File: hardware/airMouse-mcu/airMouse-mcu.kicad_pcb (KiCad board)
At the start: 2 copper layers, 126 parts, among them J1 DS1020-07-16VBT1A-R, J4 AT, J5 RADIO_PRG, J6 MCU_PRG, Q1 IRLML6346, SW50 KEY, SW51 KEY, SW52 KEY, SW53 KEY, SW54 KEY, SW55 KEY, SW56 KEY, SW57 KEY, SW58 KEY, SW59 KEY, SW60 KEY, U1 STM32G071RBTx, U2 AP1603, U3 ESP32-C3-WROOM-02U, U4 LSM6DS3

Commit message: add mouse pcb
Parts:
- removed D12: STBY, LED_SMD:LED_0603_1608Metric
- removed D13: BT, LED_SMD:LED_0603_1608Metric
- removed D43: LOW_BAT, LED_SMD:LED_0603_1608Metric
- removed R53, R54, R55, R56, R58, R59: 10k, Resistor_SMD:R_0603_1608Metric
- removed R57: 2k2, Resistor_SMD:R_0603_1608Metric
- removed R60, R61: 0R, Resistor_SMD:R_0603_1608Metric
- removed SW50, SW51, SW52, SW53, SW54, SW55, SW56, SW57, SW58, SW59, SW60: KEY, airMouseLib:TL3315NF100Q
- added D2: BT, LED_SMD:LED_0603_1608Metric, F.Cu at (123.4, 90.2)
- added D3: LOW_BAT, LED_SMD:LED_0603_1608Metric, F.Cu at (123.4, 92.8)
- added D4: STBY, LED_SMD:LED_0603_1608Metric, F.Cu at (123.4, 95.3)
- added J2: RADIO_PRG, Connector_JST:JST_ZH_S3B-ZR-SM4A-TF_1x03-1MP_P1.50mm_Horizontal, F.Cu at (131.1, 91.5)
- added J3: AT, Connector_JST:JST_ZH_S3B-ZR-SM4A-TF_1x03-1MP_P1.50mm_Horizontal, F.Cu at (131.1, 100.5)
- added SW1: KEY, airMouseLib:TL3315NF100Q, F.Cu at (149.8, 91.2)
- C11: value 100n -> 4u7; footprint Capacitor_SMD:C_0603_1608Metric -> Capacitor_SMD:C_0805_2012Metric
- C13, C9: value 100n -> 1u
- C15: value 100n -> 10u; footprint Capacitor_SMD:C_0603_1608Metric -> Capacitor_SMD:C_0805_2012Metric
- C2, C7: value 100n -> 47u; footprint Capacitor_SMD:C_0603_1608Metric -> Capacitor_SMD:CP_Elec_6.3x5.8
- C27: value 4u7 -> 100n; footprint Capacitor_SMD:C_0805_2012Metric -> Capacitor_SMD:C_0603_1608Metric
- C28, C30: value 1u -> 100n
- C3, C4: value 47u -> 100n; footprint Capacitor_SMD:CP_Elec_6.3x5.8 -> Capacitor_SMD:C_0603_1608Metric
- C32: value 10u -> 100n; footprint Capacitor_SMD:C_0805_2012Metric -> Capacitor_SMD:C_0603_1608Metric
- J1: value DS1020-07-16VBT1A-R -> MCU_PRG; footprint airMouseLib:DS1020-07-16VBT1A-R -> Connector_JST:JST_ZH_S5B-ZR-SM4A-TF_1x05-1MP_P1.50mm_Horizontal
- J4: value AT -> DS1020-07-16VBT1A-R; footprint Connector_JST:JST_ZH_S3B-ZR-SM4A-TF_1x03-1MP_P1.50mm_Horizontal -> airMouseLib:DS1020-07-16VBT1A-R
- J5: value RADIO_PRG -> DS1020-07-10VBT1A-R; footprint Connector_JST:JST_ZH_S3B-ZR-SM4A-TF_1x03-1MP_P1.50mm_Horizontal -> airMouseLib:DS1020-07-10VBT1A-R
- J6: value MCU_PRG -> Conn_01x04_MountingPin; footprint Connector_JST:JST_ZH_S5B-ZR-SM4A-TF_1x05-1MP_P1.50mm_Horizontal -> airMouseLib:DS1020-07-4VBT1A-R
- R1, R15, R2: value 100R -> 10k
- R10, R8: value 10k -> 4k7
- R12, R17: value 10k -> 2k2
- R13, R14: value 100R -> 2k2
- R18, R19, R20, R21, R22: value 10k -> 100R
- R3, R4: value 10k -> 0R
- R46, R47, R48: value 2k2 -> 10k
- R51, R52: value 4k7 -> 10k
- R6: value 10k -> 1k
- U1: value STM32G071RBTx -> LSM6DS3; footprint Package_QFP:LQFP-64_10x10mm_P0.5mm -> Package_LGA:LGA-14_3x2.5mm_P0.5mm_LayoutBorder3x4y
- U3: value ESP32-C3-WROOM-02U -> STM32G071RBTx; footprint RF_Module:ESP32-C3-WROOM-02U -> Package_QFP:LQFP-64_10x10mm_P0.5mm
- U4: value LSM6DS3 -> ESP32-C3-WROOM-02U; footprint Package_LGA:LGA-14_3x2.5mm_P0.5mm_LayoutBorder3x4y -> RF_Module:ESP32-C3-WROOM-02U
- moved TP1 107.4 mm to (122.9, 104.2)
- moved TP2 107.4 mm to (122.9, 107.2)
- moved C3 104.8 mm to (107.3, 92.6)
- moved C1 104.3 mm to (107.3, 90.1)
- moved C5 104.3 mm to (107.3, 97.7)
- moved J4 89.9 mm to (133.5, 138.2)
- moved R43 89.1 mm to (115.4, 121.7)
- moved R44 89.1 mm to (115.4, 124.2)
- moved R45 89.1 mm to (115.4, 126.7)
- moved C33 77.7 mm to (111.3, 126.7)
- moved C34 77.7 mm to (111.3, 129.2)
- moved C30 75.2 mm to (107.3, 131.7)
- moved C28 75.2 mm to (107.3, 126.7)
- moved C29 75.2 mm to (107.3, 129.2)
- moved C35 74.7 mm to (111.3, 131.7)
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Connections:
- C10 pad 1: /COL7 -> +3V3
- C11 pad 1: /COL5 -> +3V3
- C12 pad 1: /COL4 -> /ADC
- C13 pad 1: /COL3 -> /ESP_RST
- C14 pad 1: /COL2 -> +3V3
- C15 pad 1: /COL1 -> +3V3
- C16 pad 1: /mouse/MOUSE_RB -> /COL10
- C17 pad 1: /mouse/MOUSE_MB -> /COL9
- C18 pad 1: /mouse/MOUSE_LB -> /COL8
- C19 pad 1: /mouse/MOUSE_UP -> /COL7
- C2 pad 1: Net-(U2-REF) -> /BAT+
- C20 pad 1: /mouse/MOUSE_DN -> /COL6
- C21 pad 1: /mouse/MOUSE_FWD -> /COL5
- C22 pad 1: /mouse/MOUSE_BACK -> /COL4
- C23 pad 1: /mouse/MOUSE_DPI -> /COL3
- C24 pad 1: /mouse/MOUSE_PRC -> /COL2
- C25 pad 1: /mouse/MOUSE_HOME -> /COL1
- C26 pad 1: +3V3 -> /mouse/MOUSE_HOME
- C27 pad 1: +3V3 -> /mouse/MOUSE_PRC
- C28 pad 1: +3V3 -> /mouse/MOUSE_DPI
- C29 pad 1: Net-(U1-VREF+) -> /mouse/MOUSE_BACK
- C3 pad 1: /BAT+ -> +3V3
- C30 pad 1: /ESP_RST -> /mouse/MOUSE_FWD
- C31 pad 1: +3V3 -> /mouse/MOUSE_DN
- C32 pad 1: +3V3 -> /mouse/MOUSE_UP
- C33 pad 1: +3V3 -> /mouse/MOUSE_RB
- C34 pad 1: +3V3 -> /mouse/MOUSE_MB
- C35 pad 1: /BAT+ -> /mouse/MOUSE_LB
- C4 pad 1: +3V3 -> Net-(U2-REF)
- C6 pad 1: /COL6 -> +3V3
- C7 pad 1: /COL10 -> +3V3
- C8 pad 1: /COL9 -> Net-(U3-VREF+)
- C9 pad 1: /COL8 -> +3V3
- FB1 pad 2: Net-(U1-VREF+) -> Net-(U3-VREF+)
- J1 pad 1: /Keyboard/ROW5 -> +3V3
- J1 pad 2: /Keyboard/ROW4 -> /SWDCLK
- J1 pad 3: /Keyboard/ROW3 -> GND
- J1 pad 4: /Keyboard/ROW2 -> /SWDIO
- J1 pad 5: /Keyboard/ROW1 -> /RST
- J4 pad 1: /AT_MCU_TX -> /Keyboard/ROW5
- J4 pad 2: /AT_MCU_RX -> /Keyboard/ROW4
- J4 pad 3: GND -> /Keyboard/ROW3
- J5 pad 1: /PRG_ESP_RX -> GND
- J5 pad 2: /PRG_ESP_TX -> /mouse/HOME
- J5 pad 3: GND -> /mouse/PRECISION
- J6 pad 1: +3V3 -> GND
- J6 pad 2: /SWDCLK -> /mouse/BACK
- J6 pad 3: GND -> /mouse/FWD
- J6 pad 4: /SWDIO -> +3V3
- R1 pad 1: /Keyboard/KEY_ROW1 -> +3V3
- R1 pad 2: /Keyboard/ROW1 -> Net-(U1-CS)
- R10 pad 2: /Keyboard/COL8 -> /SCL
- R11 pad 2: /Keyboard/COL9 -> Net-(U4-IO8)
- R12 pad 1: +3V3 -> Net-(D2-K)
- R12 pad 2: /Keyboard/COL10 -> GND
- R13 pad 1: /Keyboard/KEY_ROW3 -> Net-(D3-K)
- R13 pad 2: /Keyboard/ROW3 -> GND
- R14 pad 1: /Keyboard/KEY_ROW4 -> Net-(D4-K)
- R14 pad 2: /Keyboard/ROW4 -> GND
- R15 pad 1: /Keyboard/KEY_ROW5 -> +3V3
- R15 pad 2: /Keyboard/ROW5 -> Net-(U4-IO2)
- R16 pad 1: /Keyboard/COL1 -> +3V3
- R16 pad 2: /COL1 -> /ESP_RST
- R17 pad 1: /Keyboard/COL2 -> Net-(LD1-A)
- R17 pad 2: /COL2 -> Net-(SW1-A)
- R18 pad 1: /Keyboard/COL3 -> /Keyboard/KEY_ROW1
- R18 pad 2: /COL3 -> /Keyboard/ROW1
- R19 pad 1: /Keyboard/COL4 -> /Keyboard/KEY_ROW2
- R19 pad 2: /COL4 -> /Keyboard/ROW2
- R2 pad 1: /Keyboard/KEY_ROW2 -> Net-(U1-SDO/SA0)
- R2 pad 2: /Keyboard/ROW2 -> GND
- R20 pad 1: /Keyboard/COL5 -> /Keyboard/KEY_ROW3
- R20 pad 2: /COL5 -> /Keyboard/ROW3
- R21 pad 1: /Keyboard/COL6 -> /Keyboard/KEY_ROW4
- R21 pad 2: /COL6 -> /Keyboard/ROW4
- R22 pad 1: /Keyboard/COL7 -> /Keyboard/KEY_ROW5
- R22 pad 2: /COL7 -> /Keyboard/ROW5
- R23 pad 1: /Keyboard/COL8 -> +3V3
- R23 pad 2: /COL8 -> /Keyboard/COL1
- R24 pad 1: /Keyboard/COL9 -> +3V3
- R24 pad 2: /COL9 -> /Keyboard/COL2
- R25 pad 1: /Keyboard/COL10 -> +3V3
- R25 pad 2: /COL10 -> /Keyboard/COL3
- R26 pad 2: /mouse/LMB -> /Keyboard/COL4
- R27 pad 2: /mouse/MMB -> /Keyboard/COL5
- R28 pad 2: /mouse/RMB -> /Keyboard/COL6
- R29 pad 1: /mouse/LMB -> +3V3
- R29 pad 2: /mouse/MOUSE_LB -> /Keyboard/COL7
- R3 pad 1: +3V3 -> /SDX
- R3 pad 2: /Keyboard/COL1 -> GND
- R30 pad 1: /mouse/MMB -> +3V3
- R30 pad 2: /mouse/MOUSE_MB -> /Keyboard/COL8
- R31 pad 1: /mouse/RMB -> +3V3
- R31 pad 2: /mouse/MOUSE_RB -> /Keyboard/COL9
- R32 pad 1: /mouse/SCRLUP -> +3V3
- R32 pad 2: /mouse/MOUSE_UP -> /Keyboard/COL10
- R33 pad 1: /mouse/SCRLDN -> /Keyboard/COL1
- R33 pad 2: /mouse/MOUSE_DN -> /COL1
- R34 pad 1: /mouse/FWD -> /Keyboard/COL2
- R34 pad 2: /mouse/MOUSE_FWD -> /COL2
- R35 pad 1: /mouse/BACK -> /Keyboard/COL3
- R35 pad 2: /mouse/MOUSE_BACK -> /COL3
- R36 pad 1: /mouse/DPI -> /Keyboard/COL4
- R36 pad 2: /mouse/MOUSE_DPI -> /COL4
- R37 pad 1: /mouse/PRECISION -> /Keyboard/COL5
- R37 pad 2: /mouse/MOUSE_PRC -> /COL5
- R38 pad 1: +3V3 -> /Keyboard/COL6
- R38 pad 2: /mouse/SCRLUP -> /COL6
- R39 pad 1: +3V3 -> /Keyboard/COL7
- R39 pad 2: /mouse/SCRLDN -> /COL7
- R4 pad 1: +3V3 -> /SCX
- R4 pad 2: /Keyboard/COL2 -> GND
- R40 pad 1: +3V3 -> /Keyboard/COL8
- R40 pad 2: /mouse/FWD -> /COL8
- R41 pad 1: +3V3 -> /Keyboard/COL9
- R41 pad 2: /mouse/BACK -> /COL9
- R42 pad 1: +3V3 -> /Keyboard/COL10
- R42 pad 2: /mouse/DPI -> /COL10
- R43 pad 1: +3V3 -> /mouse/LMB
- R43 pad 2: /mouse/PRECISION -> /mouse/MOUSE_LB
- R44 pad 1: /mouse/HOME -> /mouse/MMB
- R44 pad 2: /mouse/MOUSE_HOME -> /mouse/MOUSE_MB
- R45 pad 1: +3V3 -> /mouse/RMB
- R45 pad 2: /mouse/HOME -> /mouse/MOUSE_RB
- R46 pad 1: Net-(D12-K) -> /mouse/SCRLUP
- R46 pad 2: GND -> /mouse/MOUSE_UP
- R47 pad 1: Net-(D13-K) -> /mouse/SCRLDN
- R47 pad 2: GND -> /mouse/MOUSE_DN
- R48 pad 1: Net-(D43-K) -> /mouse/DPI
- R48 pad 2: GND -> /mouse/MOUSE_FWD
- R49 pad 1: +3V3 -> /mouse/PRECISION
- R49 pad 2: /RST -> /mouse/MOUSE_BACK
- R5 pad 2: /Keyboard/COL3 -> /RST
- R50 pad 1: /SWDCLK -> /mouse/HOME
- R50 pad 2: GND -> /mouse/MOUSE_DPI
- R51 pad 1: +3V3 -> /mouse/FWD
- R51 pad 2: /SDA -> /mouse/MOUSE_PRC
- R52 pad 1: +3V3 -> /mouse/BACK
- R52 pad 2: /SCL -> /mouse/MOUSE_HOME
- R6 pad 1: +3V3 -> /ADC
- R6 pad 2: /Keyboard/COL4 -> /BAT+
- R7 pad 1: +3V3 -> /SWDCLK
- R7 pad 2: /Keyboard/COL5 -> GND
- R8 pad 2: /Keyboard/COL6 -> /SDA
- R9 pad 2: /Keyboard/COL7 -> /ESP_BOOT
- U1 pad 1: /mouse/MOUSE_FWD -> Net-(U1-SDO/SA0)
- U1 pad 12: /RST -> Net-(U1-CS)
- U1 pad 13: unconnected-(U1-PC0-Pad13) -> /SCL
- U1 pad 14: unconnected-(U1-PC1-Pad14) -> /SDA
- U1 pad 2: /mouse/MOUSE_BACK -> /SDX
- U1 pad 3: /mouse/MOUSE_DPI -> /SCX
- U1 pad 4: /mouse/MOUSE_PRC -> /GYRO_INT
- U1 pad 5: /mouse/MOUSE_HOME -> +3V3
- U1 pad 6: +3V3 -> GND
- U1 pad 7: Net-(U1-VREF+) -> GND
- U1 pad 9: GND -> unconnected-(U1-INT2-Pad9)
- U3 pad 1: +3V3 -> /mouse/MOUSE_FWD
- U3 pad 11: /PRG_ESP_RX -> unconnected-(U3-PF1-Pad11)
- U3 pad 12: /PRG_ESP_TX -> /RST
- U3 pad 16: Net-(U3-IO2) -> unconnected-(U3-PC3-Pad16)
- U3 pad 17: unconnected-(U3-IO1-Pad17) -> /GYRO_INT
- U3 pad 18: unconnected-(U3-IO0-Pad18) -> Net-(D2-A)
- U3 pad 19: GND -> /DBG_TX
- U3 pad 2: /ESP_RST -> /mouse/MOUSE_BACK
- U3 pad 3: unconnected-(U3-IO4-Pad3) -> /mouse/MOUSE_DPI
- U3 pad 4: unconnected-(U3-IO5-Pad4) -> /mouse/MOUSE_PRC
- U3 pad 5: /AT_MCU_TX -> /mouse/MOUSE_HOME
- U3 pad 6: /AT_MCU_RX -> +3V3
- U3 pad 7: Net-(U3-IO8) -> Net-(U3-VREF+)
- U3 pad 8: /ESP_BOOT -> +3V3
- U4 pad 1: Net-(U4-SDO/SA0) -> +3V3
- U4 pad 11: unconnected-(U4-NC-Pad11) -> /PRG_ESP_RX
- U4 pad 12: Net-(U4-CS) -> /PRG_ESP_TX
- U4 pad 13: /SCL -> unconnected-(U4-IO18-Pad13)
- U4 pad 14: /SDA -> unconnected-(U4-IO19-Pad14)
- U4 pad 2: /SDX -> /ESP_RST
- U4 pad 3: /SCX -> unconnected-(U4-IO4-Pad3)
- U4 pad 4: /GYRO_INT -> unconnected-(U4-IO5-Pad4)
- U4 pad 5: +3V3 -> /AT_MCU_TX
- U4 pad 6: GND -> /AT_MCU_RX
- U4 pad 7: GND -> Net-(U4-IO8)
- U4 pad 8: +3V3 -> /ESP_BOOT
- U4 pad 9: unconnected-(U4-INT2-Pad9) -> GND
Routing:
- net +3V3: track 35.5 -> 0.00 mm, vias 2 -> 0
- net /Keyboard/COL5: track 18.4 -> 0.00 mm, vias 2 -> 0
- net /Keyboard/COL3: track 8.60 -> 0.00 mm, vias 2 -> 0
- net /Keyboard/COL8: track 7.17 -> 0.00 mm, vias 2 -> 0
- net /Keyboard/COL9: track 6.36 -> 0.00 mm, vias 2 -> 0
- net /Keyboard/ROW5: track 6.19 -> 0.00 mm
- net /Keyboard/COL2: track 6.17 -> 0.00 mm, vias 2 -> 0
- net /Keyboard/COL1: track 6.17 -> 0.00 mm, vias 2 -> 0
- net /Keyboard/COL7: track 5.53 -> 0.00 mm, vias 2 -> 0
- net /Keyboard/COL6: track 4.75 -> 0.00 mm, vias 2 -> 0
- net /Keyboard/COL4: track 4.75 -> 0.00 mm, vias 2 -> 0
- net /Keyboard/COL10: track 4.75 -> 0.00 mm, vias 2 -> 0
- net /Keyboard/ROW3: track 4.22 -> 0.00 mm
- net /Keyboard/ROW2: track 1.50 -> 0.00 mm
- net /COL8: track 1.45 -> 0.00 mm
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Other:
- board text added: "airMouse-mouse RC1"

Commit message: thumb pcb
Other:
- board text added: "airMouse-mcu"
- board text removed: "airMouse-mouse RC1"
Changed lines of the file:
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@@
 		)
 	)
-	(gr_text "airMouse-mouse RC1"
-		(at 134.1 114.1 -0)
+	(gr_text "airMouse-mcu"
+		(at 134.1 114.1 0)
 		(layer "B.SilkS")
 		(effects

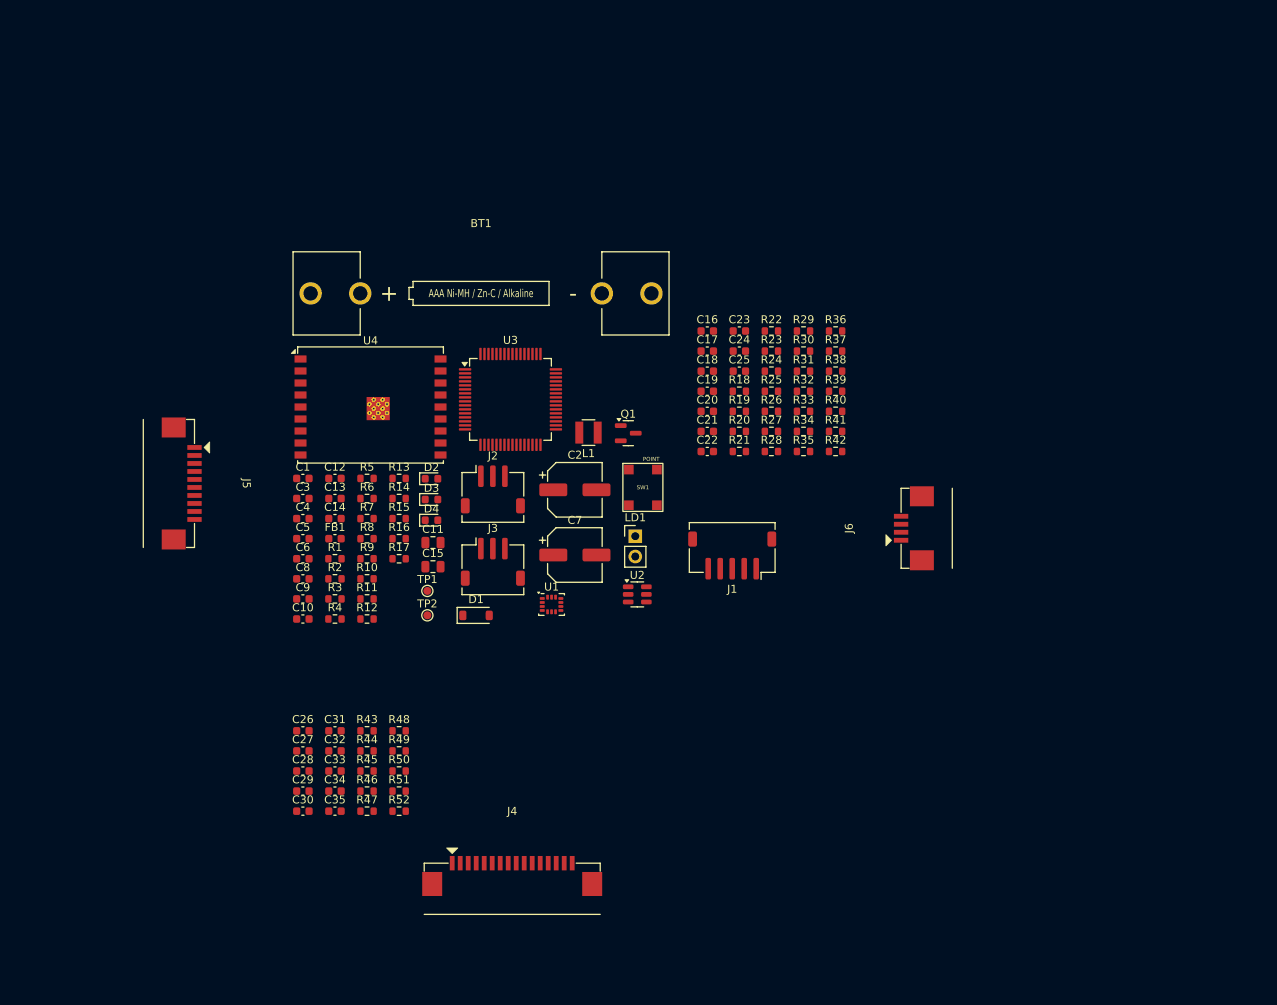
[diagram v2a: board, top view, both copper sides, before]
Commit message: components placed on mcu board
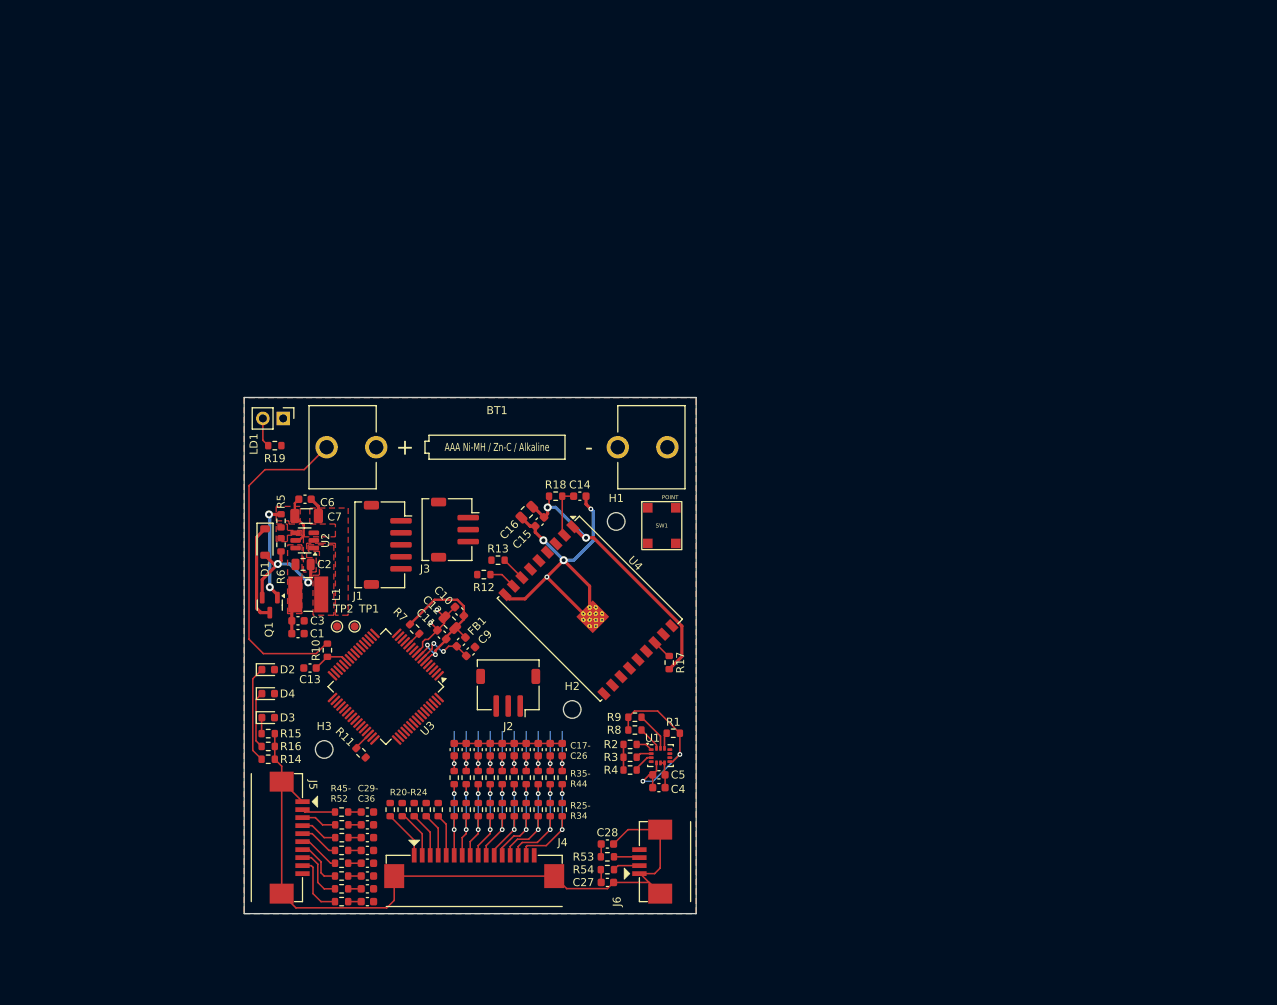
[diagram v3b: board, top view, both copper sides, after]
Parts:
- removed C8: 100n, Capacitor_SMD:C_0603_1608Metric
- added C36: 100n, Capacitor_SMD:C_0603_1608Metric, F.Cu at (115.4, 143.0)
- added H1: MountingHole, MountingHole:MountingHole_2.2mm_M2_ISO14580, F.Cu at (146.5, 95.5)
- added H2: MountingHole, MountingHole:MountingHole_2.2mm_M2_ISO14580, F.Cu at (141.0, 119.0)
- added H3: MountingHole, MountingHole:MountingHole_2.2mm_M2_ISO14580, F.Cu at (110.0, 124.0)
- added Logo1: ~, airMouseLib:Bart's Design 30mm, B.Cu at (128.3, 111.7)
- added R53: 10k, Resistor_SMD:R_0603_1608Metric, F.Cu at (145.4, 137.4)
- added R54: 10k, Resistor_SMD:R_0603_1608Metric, F.Cu at (145.4, 139.0)
- C10, C14: value 100n -> 1u
- C11: value 4u7 -> 100n; footprint Capacitor_SMD:C_0805_2012Metric -> Capacitor_SMD:C_0603_1608Metric
- C12: value 100n -> 4u7; footprint Capacitor_SMD:C_0603_1608Metric -> Capacitor_SMD:C_0805_2012Metric
- C13, C9: value 1u -> 100n
- C15: value 10u -> 100n; footprint Capacitor_SMD:C_0805_2012Metric -> Capacitor_SMD:C_0603_1608Metric
- C16: value 100n -> 10u; footprint Capacitor_SMD:C_0603_1608Metric -> Capacitor_SMD:C_0805_2012Metric
- C2: value 47u -> 4u7; footprint Capacitor_SMD:CP_Elec_6.3x5.8 -> Capacitor_SMD:C_0805_2012Metric
- C7: value 47u -> 10u; footprint Capacitor_SMD:CP_Elec_6.3x5.8 -> Capacitor_SMD:C_1206_3216Metric
- L1: value 22u / WLPN303010M220PB -> 4u7; footprint Inductor_SMD:L_Abracon_ASPI-3012S -> Inductor_SMD:L_Ferrocore_DLG-0403
- R10: value 4k7 -> 1k
- R12, R13, R17: value 2k2 -> 10k
- R15, R16: value 10k -> 2k2
- R18: value 100R -> 10k
- R19: value 100R -> 2k2
- R23, R24: value 10k -> 100R
- R5: value 10k -> 976k
- R6: value 1k -> 562k
- R9: value 10k -> 4k7
- U2: value AP1603 -> MCP1640CT-I/CHY
- moved R22 74.7 mm to (121.2, 131.5), turned to -90 degrees
- moved R23 73.6 mm to (119.8, 131.5), turned to -90 degrees
- moved R24 72.6 mm to (118.2, 131.5), turned to -90 degrees
- moved R29 69.9 mm to (133.8, 131.5), turned to -90 degrees
- moved R30 68.6 mm to (132.3, 131.5), turned to -90 degrees
- moved R31 67.4 mm to (130.8, 131.5), turned to -90 degrees
- moved R36 66.3 mm to (138.2, 127.5), turned to 90 degrees
- moved R32 66.2 mm to (129.3, 131.5), turned to -90 degrees
- moved R33 65.2 mm to (127.8, 131.5), turned to -90 degrees
- moved R37 65.0 mm to (136.8, 127.5), turned to 90 degrees
- moved R34 64.4 mm to (126.2, 131.5), turned to -90 degrees
- moved R38 63.9 mm to (135.2, 127.5), turned to 90 degrees
- moved R39 62.8 mm to (133.8, 127.5), turned to 90 degrees
- moved R40 61.9 mm to (132.2, 127.5), turned to 90 degrees
- moved R41 61.1 mm to (130.8, 127.5), turned to 90 degrees
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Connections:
- net Net-(D2-A) renamed /CONN
- net Net-(D3-A) renamed /LOW_BAT
- net Net-(D4-A) renamed /STBY
- C12 pad 1: /ADC -> +3V3
- C13 pad 1: /ESP_RST -> /ADC
- C14 pad 1: +3V3 -> /ESP_RST
- C16 pad 1: /COL10 -> +3V3
- C17 pad 1: /COL9 -> /COL10
- C18 pad 1: /COL8 -> /COL9
- C19 pad 1: /COL7 -> /COL8
- C20 pad 1: /COL6 -> /COL7
- C21 pad 1: /COL5 -> /COL6
- C22 pad 1: /COL4 -> /COL5
- C23 pad 1: /COL3 -> /COL4
- C24 pad 1: /COL2 -> /COL3
- C25 pad 1: /COL1 -> /COL2
- C26 pad 1: /mouse/MOUSE_HOME -> /COL1
- C27 pad 1: /mouse/MOUSE_PRC -> /mouse/MOUSE_HOME
- C28 pad 1: /mouse/MOUSE_DPI -> /mouse/MOUSE_PRC
- C29 pad 1: /mouse/MOUSE_BACK -> /mouse/MOUSE_DPI
- C3 pad 1: +3V3 -> /BAT+
- C30 pad 1: /mouse/MOUSE_FWD -> /mouse/MOUSE_BACK
- C31 pad 1: /mouse/MOUSE_DN -> /mouse/MOUSE_FWD
- C32 pad 1: /mouse/MOUSE_UP -> /mouse/MOUSE_DN
- C33 pad 1: /mouse/MOUSE_RB -> /mouse/MOUSE_UP
- C34 pad 1: /mouse/MOUSE_MB -> /mouse/MOUSE_RB
- C35 pad 1: /mouse/MOUSE_LB -> /mouse/MOUSE_MB
- C4 pad 1: Net-(U2-REF) -> +3V3
- C9 pad 1: +3V3 -> Net-(U3-VREF+)
- L1 pad 2: Net-(U2-LX) -> /SW
- R10 pad 1: +3V3 -> /ADC
- R10 pad 2: /SCL -> /BAT+
- R11 pad 1: +3V3 -> /SWDCLK
- R11 pad 2: Net-(U4-IO8) -> GND
- R12 pad 1: Net-(D2-K) -> +3V3
- R12 pad 2: GND -> /ESP_BOOT
- R13 pad 1: Net-(D3-K) -> +3V3
- R13 pad 2: GND -> Net-(U4-IO8)
- R14 pad 1: Net-(D4-K) -> Net-(D2-K)
- R15 pad 1: +3V3 -> Net-(D3-K)
- R15 pad 2: Net-(U4-IO2) -> GND
- R16 pad 1: +3V3 -> Net-(D4-K)
- R16 pad 2: /ESP_RST -> GND
- R17 pad 1: Net-(LD1-A) -> +3V3
- R17 pad 2: Net-(SW1-A) -> Net-(U4-IO2)
- R18 pad 1: /Keyboard/KEY_ROW1 -> +3V3
- R18 pad 2: /Keyboard/ROW1 -> /ESP_RST
- R19 pad 1: /Keyboard/KEY_ROW2 -> Net-(LD1-A)
- R19 pad 2: /Keyboard/ROW2 -> Net-(SW1-A)
- R20 pad 1: /Keyboard/KEY_ROW3 -> /Keyboard/KEY_ROW1
- R20 pad 2: /Keyboard/ROW3 -> /Keyboard/ROW1
- R21 pad 1: /Keyboard/KEY_ROW4 -> /Keyboard/KEY_ROW2
- R21 pad 2: /Keyboard/ROW4 -> /Keyboard/ROW2
- R22 pad 1: /Keyboard/KEY_ROW5 -> /Keyboard/KEY_ROW3
- R22 pad 2: /Keyboard/ROW5 -> /Keyboard/ROW3
- R23 pad 1: +3V3 -> /Keyboard/KEY_ROW4
- R23 pad 2: /Keyboard/COL1 -> /Keyboard/ROW4
- R24 pad 1: +3V3 -> /Keyboard/KEY_ROW5
- R24 pad 2: /Keyboard/COL2 -> /Keyboard/ROW5
- R25 pad 2: /Keyboard/COL3 -> /Keyboard/COL1
- R26 pad 2: /Keyboard/COL4 -> /Keyboard/COL2
- R27 pad 2: /Keyboard/COL5 -> /Keyboard/COL3
- R28 pad 2: /Keyboard/COL6 -> /Keyboard/COL4
- R29 pad 2: /Keyboard/COL7 -> /Keyboard/COL5
- R30 pad 2: /Keyboard/COL8 -> /Keyboard/COL6
- R31 pad 2: /Keyboard/COL9 -> /Keyboard/COL7
- R32 pad 2: /Keyboard/COL10 -> /Keyboard/COL8
- R33 pad 1: /Keyboard/COL1 -> +3V3
- R33 pad 2: /COL1 -> /Keyboard/COL9
- R34 pad 1: /Keyboard/COL2 -> +3V3
- R34 pad 2: /COL2 -> /Keyboard/COL10
- R35 pad 1: /Keyboard/COL3 -> /Keyboard/COL1
- R35 pad 2: /COL3 -> /COL1
- R36 pad 1: /Keyboard/COL4 -> /Keyboard/COL2
- R36 pad 2: /COL4 -> /COL2
- R37 pad 1: /Keyboard/COL5 -> /Keyboard/COL3
- R37 pad 2: /COL5 -> /COL3
- R38 pad 1: /Keyboard/COL6 -> /Keyboard/COL4
- R38 pad 2: /COL6 -> /COL4
- R39 pad 1: /Keyboard/COL7 -> /Keyboard/COL5
- R39 pad 2: /COL7 -> /COL5
- R40 pad 1: /Keyboard/COL8 -> /Keyboard/COL6
- R40 pad 2: /COL8 -> /COL6
- R41 pad 1: /Keyboard/COL9 -> /Keyboard/COL7
- R41 pad 2: /COL9 -> /COL7
- R42 pad 1: /Keyboard/COL10 -> /Keyboard/COL8
- R42 pad 2: /COL10 -> /COL8
- R43 pad 1: /mouse/LMB -> /Keyboard/COL9
- R43 pad 2: /mouse/MOUSE_LB -> /COL9
- R44 pad 1: /mouse/MMB -> /Keyboard/COL10
- R44 pad 2: /mouse/MOUSE_MB -> /COL10
- R45 pad 1: /mouse/RMB -> /mouse/LMB
- R45 pad 2: /mouse/MOUSE_RB -> /mouse/MOUSE_LB
- R46 pad 1: /mouse/SCRLUP -> /mouse/MMB
- R46 pad 2: /mouse/MOUSE_UP -> /mouse/MOUSE_MB
- R47 pad 1: /mouse/SCRLDN -> /mouse/RMB
- R47 pad 2: /mouse/MOUSE_DN -> /mouse/MOUSE_RB
- R48 pad 1: /mouse/DPI -> /mouse/SCRLUP
- R48 pad 2: /mouse/MOUSE_FWD -> /mouse/MOUSE_UP
- R49 pad 1: /mouse/PRECISION -> /mouse/SCRLDN
- R49 pad 2: /mouse/MOUSE_BACK -> /mouse/MOUSE_DN
- R5 pad 2: /RST -> /FB
- R50 pad 1: /mouse/HOME -> /mouse/DPI
- R50 pad 2: /mouse/MOUSE_DPI -> /mouse/MOUSE_FWD
- R51 pad 1: /mouse/FWD -> /mouse/PRECISION
- R51 pad 2: /mouse/MOUSE_PRC -> /mouse/MOUSE_BACK
- R52 pad 1: /mouse/BACK -> /mouse/HOME
- R52 pad 2: /mouse/MOUSE_HOME -> /mouse/MOUSE_DPI
- R6 pad 1: /ADC -> /FB
- R6 pad 2: /BAT+ -> GND
- R7 pad 1: /SWDCLK -> +3V3
- R7 pad 2: GND -> /RST
- R9 pad 2: /ESP_BOOT -> /SCL
- U2 pad 1: +3V3 -> /SW
- U2 pad 3: Net-(U2-REF) -> /BAT+
- U2 pad 4: Net-(U2-LX) -> /FB
- U2 pad 6: +3V3 -> /BAT+
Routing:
- net GND: track 0.00 -> 186.1 mm, vias 0 -> 8
- net +3V3: track 0.00 -> 102.4 mm, vias 0 -> 8
- net /BAT+: track 0.00 -> 47.0 mm
- net /Keyboard/COL1: track 0.00 -> 13.8 mm, vias 0 -> 2
- net /Keyboard/COL2: track 0.00 -> 13.3 mm, vias 0 -> 2
- net /Keyboard/COL3: track 0.00 -> 12.8 mm, vias 0 -> 2
- net /BAT-: track 0.00 -> 12.3 mm
- net /Keyboard/COL4: track 0.00 -> 12.2 mm, vias 0 -> 2
- net Net-(D2-K): track 0.00 -> 12.1 mm
- net /Keyboard/COL5: track 0.00 -> 11.6 mm, vias 0 -> 2
- net /Keyboard/COL6: track 0.00 -> 11.4 mm, vias 0 -> 2
- net /Keyboard/COL9: track 0.00 -> 11.3 mm, vias 0 -> 2
- net /Keyboard/COL7: track 0.00 -> 11.2 mm, vias 0 -> 2
- net /Keyboard/COL8: track 0.00 -> 11.0 mm, vias 0 -> 2
- net /Keyboard/COL10: track 0.00 -> 10.6 mm, vias 0 -> 2
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- added copper zone on F.Cu, net +3V3
- added copper zone on F.Cu, net /BAT+
- added copper zone on F.Cu, net /FB
- added copper zone on F.Cu, net /SW
- added copper zone on B.Cu, net GND
- added copper zone on F.Cu, net GND
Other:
- board outline added: 56.5 x 64.5 mm
- board text added: "C17- C26"
- board text added: "C29- C36"
- board text added: "R20-R24"
- board text added: "R25- R34"
- board text added: "R35- R44"
- board text added: "R45- R52"

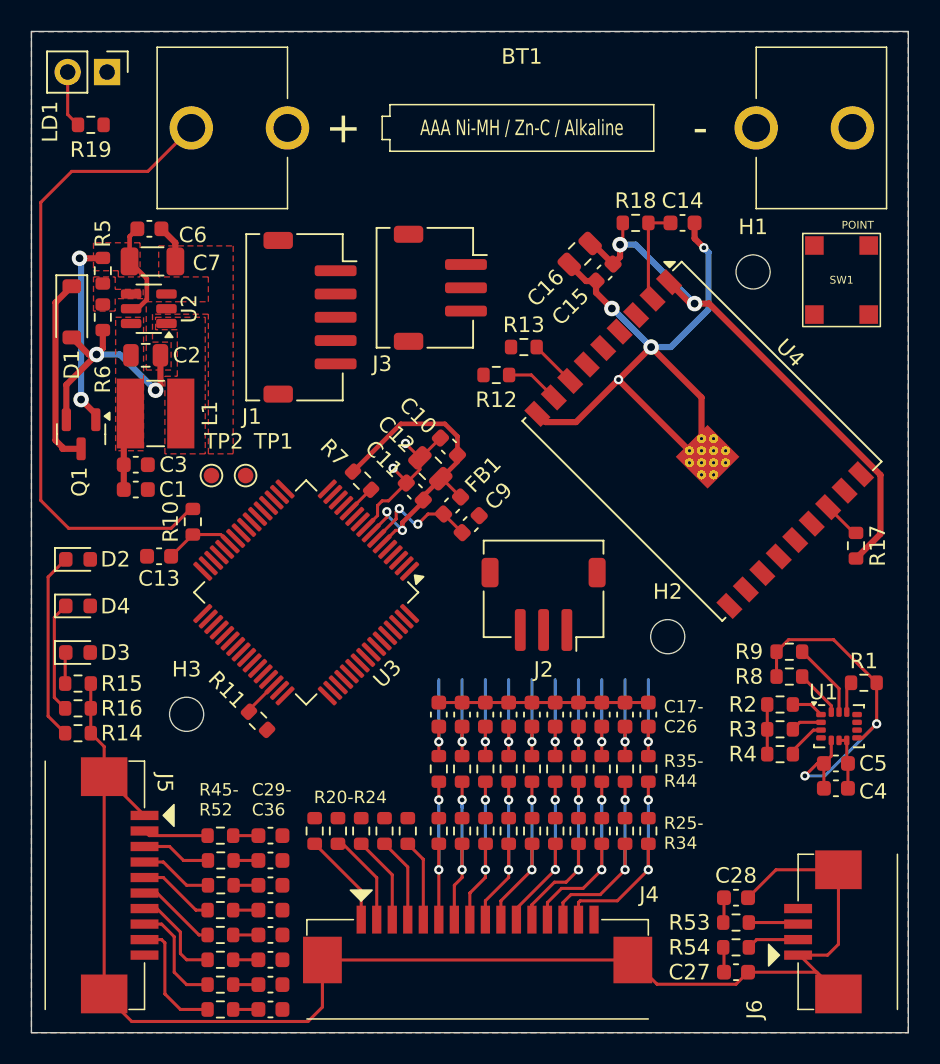
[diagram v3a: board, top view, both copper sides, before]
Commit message: add mcu board
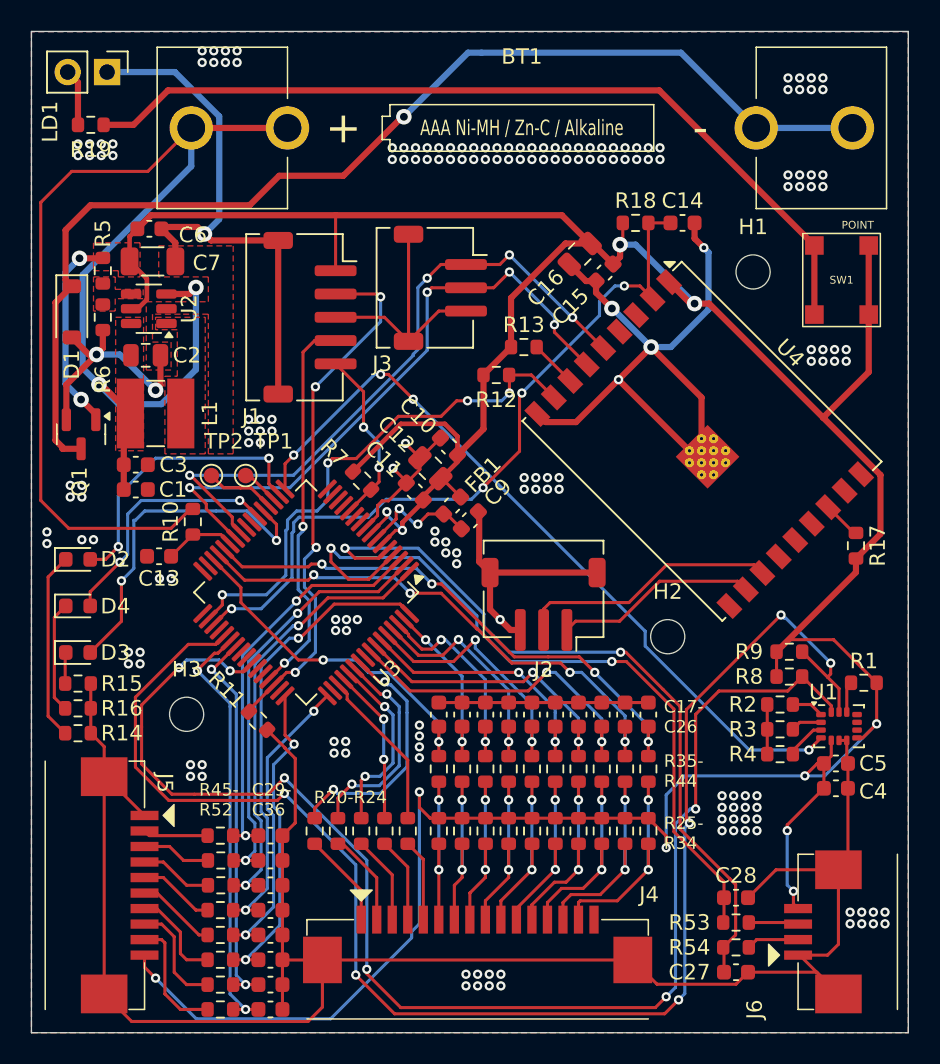
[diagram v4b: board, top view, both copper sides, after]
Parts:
- moved C9 0.25 mm to (128.2, 111.5)
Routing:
- net +3V3: track 102.4 -> 247.0 mm, vias 8 -> 13
- net GND: track 186.1 -> 280.0 mm, vias 8 -> 183
- net /SCL: track 4.87 -> 96.4 mm, vias 0 -> 6
- net /SDA: track 3.06 -> 88.5 mm, vias 0 -> 6
- net /BAT-: track 12.3 -> 73.5 mm, vias 0 -> 1
- net Net-(SW1-A): track 0.00 -> 55.5 mm
- net /GYRO_INT: track 0.00 -> 49.5 mm, vias 0 -> 4
- net /mouse/MOUSE_HOME: track 1.62 -> 48.5 mm, vias 0 -> 2
- net /mouse/MOUSE_PRC: track 1.62 -> 48.0 mm, vias 0 -> 2
- net /BAT+: track 47.0 -> 90.9 mm, vias 0 -> 2
- net /AT_MCU_TX: track 0.00 -> 42.5 mm, vias 0 -> 4
- net /ESP_RST: track 6.42 -> 48.7 mm, vias 0 -> 4
- net /AT_MCU_RX: track 0.00 -> 41.1 mm, vias 0 -> 4
- net /SWDCLK: track 2.40 -> 34.3 mm, vias 0 -> 4
- net /ESP_BOOT: track 3.48 -> 33.9 mm, vias 0 -> 4
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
